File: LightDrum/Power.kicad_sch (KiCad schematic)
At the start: 46 parts, among them Q2 BC807, U26 LM22673-SOIC, U27 LMV324, U28 LMV324, U29 LMV324, U3 LMV324, U39 74HCT2G08, U4 LMV324, U42 INA4181 A2, U43 INA4181 A2, U46 74HC02, U5 LMV324, U6 LM358, U7 OPA1652

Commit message: Add docs and gerbers for REV7
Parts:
- D6: footprint Diode_SMD:D_SMA-SMB_Universal_Handsoldering -> Diode_SMD:D_SMA
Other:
- title: POWER SUPPLY -> LightDrum
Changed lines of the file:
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@@
   (paper "A4")
   (title_block
-    (title "POWER SUPPLY")
-    (rev "REV6")
+    (title "LightDrum")
+    (rev "REV7")
     (company "Daxxn Industries")
   )
@@
       (effects (font (size 1.27 1.27)) (justify left))
     )
-    (property "Footprint" "Diode_SMD:D_SMA-SMB_Universal_Handsoldering" (id 2) (at 91.44 40.64 90)
-      (effects (font (size 1.27 1.27)) hide)
-    )
+    (property "Footprint" "Diode_SMD:D_SMA" (id 2) (at 91.44 40.64 90)
+      (effects (font (size 1.27 1.27)) hide)
+    )

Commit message: First pass over schematic (WIP)
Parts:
- removed C39: 1uF, Capacitor_SMD:C_0603_1608Metric, symbol Device:C_Small
- removed C41, C43, C45, C46, C48, C50, C53, C58, C59, C60, C86: ${D-CAP}, Capacitor_SMD:C_0603_1608Metric, symbol Device:C_Small
- removed Q2: BC807, Package_TO_SOT_SMD:SOT-23, symbol Transistor_BJT:BC807
- removed R104: 1K${RES}, Resistor_SMD:R_0805_2012Metric, symbol Device:R_Small_US
- removed R72: 2.7K${RES}, Resistor_SMD:R_0805_2012Metric, symbol Device:R_Small_US
- removed R73: 7.5K${RES}, Resistor_SMD:R_0805_2012Metric, symbol Device:R_Small_US
- removed U27, U28, U29, U3, U4, U5: LMV324, Package_SO:TSSOP-14_4.4x5mm_P0.65mm, symbol Amplifier_Operational:LMV324
- removed U46: 74HC02, Daxxn_Packages:DHVQFN14, symbol 74xx:74HC02
- removed U6: LM358, Package_SO:TSSOP-8_4.4x3mm_P0.65mm, symbol Amplifier_Operational:LM358
- removed U7: OPA1652, Package_SO:VSSOP-8_3.0x3.0mm_P0.65mm, symbol Daxxn_OPAMP:OPA1652
- added C20: 22pF, Capacitor_SMD:C_0603_1608Metric, symbol Device:C_Small
- added C21, C22: 100nF, Capacitor_SMD:C_0805_2012Metric, symbol Device:C_Small
- added C23, C24: 1uF, Capacitor_SMD:C_0805_2012Metric, symbol Device:C_Small
- added C25: 10uF, Capacitor_SMD:CP_Elec_5x5.4, symbol Device:C_Polarized_Small
- added C26: 100nF, Capacitor_SMD:C_0603_1608Metric, symbol Device:C_Small
- added L1: 2.2uH, symbol Device:L
- added L3: 22uH, Daxxn_Passives:PA4341, symbol Device:L
- added R12: 2.78K, Resistor_SMD:R_0805_2012Metric, symbol Device:R_Small_US
- added R13, R14, R17: 100K, Resistor_SMD:R_0805_2012Metric, symbol Device:R_Small_US
- added R15: 430K, Resistor_SMD:R_0805_2012Metric, symbol Device:R_Small_US
- added R16: 7.5K, Resistor_SMD:R_0805_2012Metric, symbol Device:R_Small_US
- added U3: AP3401, Package_DFN_QFN:DFN-6-1EP_2x2mm_P0.65mm_EP1x1.6mm, symbol Daxxn_Regulators:AP3401
- C49, C55, C62, C63: value ${D-CAP} -> 100nF
- L2: value 22uH -> 10uH; footprint Daxxn_Passives:PA4341 -> Capacitor_SMD:C_1210_3225Metric; now left out of the parts list
- R71: value 15K${RES} -> 15K
- U39: value 74HCT2G08 -> 74HC2G08
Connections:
- net GND: now also C21.2, C22.2, C23.2, C24.2, C25.2, C26.2, R12.1, R17.2, U3.5 (GND), U3.7 (GND)
- net PS-FB_: now also R12.2, R16.1
- net PS-SW_: now also L3.1; no longer L2.1
- net VCC: now also C25.1, C26.1, L3.2, R13.1, R14.1, R16.2, U3.3 (VIN); no longer C55.1, C62.1, C63.1, L2.2, U39.8, U42.5, U43.5
- new net: R14.2, U3.2 (PG)
- new net: R13.2, U3.1 (EN)
- new net: L1.1, U3.4 (LX)
- new net: C20.2, R15.2, R17.1, U3.6 (FB)
- new net +3V3: C20.1, C21.1, C22.1, C23.1, L1.2, L2.1, R15.1
- new net VDD: C24.1, C55.1, C62.1, C63.1, L2.2, U39.8, U42.5, U43.5
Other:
- note added: "3.3V REGULATOR"
- note added: "The new voltage is going to be 3.3V. Need to check all my ICs and confirm compatibility."
- note removed: "2.6K Would be exactly 5V but its hard to find a resistor with that value."
- note removed: "AUDIO AMP"
- note removed: "AUDIO fILTERS"
- note removed: "COUNTER"
- note removed: "ICSP Backfeed Protection"
- note removed: "OR GATE"
- note removed: "PWM MUX CONTROL"
- note removed: "TIMER"
- moved on the sheet: C55, C62, C63, U39C, U42E, U43E

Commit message: General component placement
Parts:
- C1001: renamed from C20; footprint Capacitor_SMD:C_0603_1608Metric -> Capacitor_SMD:C_0402_1005Metric
- D1001: renamed from D6; value ES2A/A -> SK36AHE3
- L1001: renamed from L1; footprint (none) -> Daxxn_Passives:LQH3NPN; now in the parts list
- L1002: renamed from L2; now in the parts list
- L1003: renamed from L3; now in the parts list
- R1001: renamed from R12; now in the parts list
- R1002: renamed from R13; footprint Resistor_SMD:R_0805_2012Metric -> Resistor_SMD:R_0402_1005Metric; now in the parts list
- R1003: renamed from R14; footprint Resistor_SMD:R_0805_2012Metric -> Resistor_SMD:R_0402_1005Metric; now in the parts list
- R1004: renamed from R15; footprint Resistor_SMD:R_0805_2012Metric -> Resistor_SMD:R_0402_1005Metric; now in the parts list
- R1005: renamed from R16; now in the parts list
- R1006: renamed from R17; footprint Resistor_SMD:R_0805_2012Metric -> Resistor_SMD:R_0402_1005Metric; now in the parts list
- U1002: renamed from U26; PartNumber (none) -> 0805-0001; SupplierPN (none) -> LM22673MRE-5.0/NOPBCT-ND
- U701: renamed from U42; PartNumber (none) -> 0815-0003
- U702: renamed from U43; PartNumber (none) -> 0815-0003
- U901: renamed from U39; PartNumber (none) -> 0802-0005
- renumbered C21 to C1002, C22 to C1003, C23 to C1004, C24 to C1005, C38 to C1006, C40 to C1007, C42 to C1008, C56 to C1009, C47 to C1010, C25 to C1011, C26 to C1012, C44 to C1013, C49 to C1014, C51 to C1015, C57 to C1016, C52 to C1017, C54 to C1018, C55 to C1019, C62 to C1020, C63 to C1021, R71 to R1007, U3 to U1001

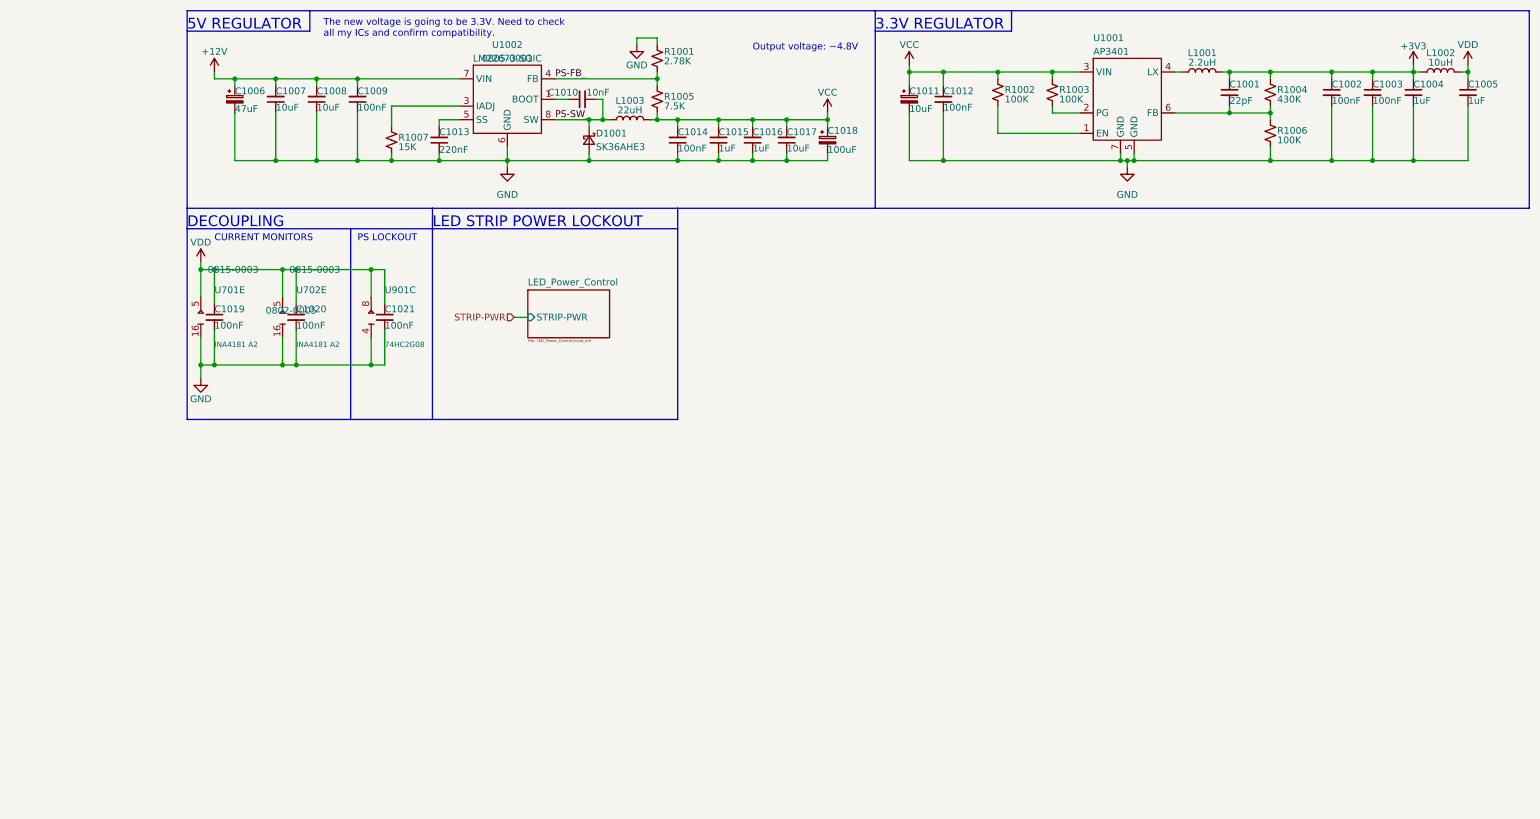
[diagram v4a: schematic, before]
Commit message: Simplify analog power supply and add some routing
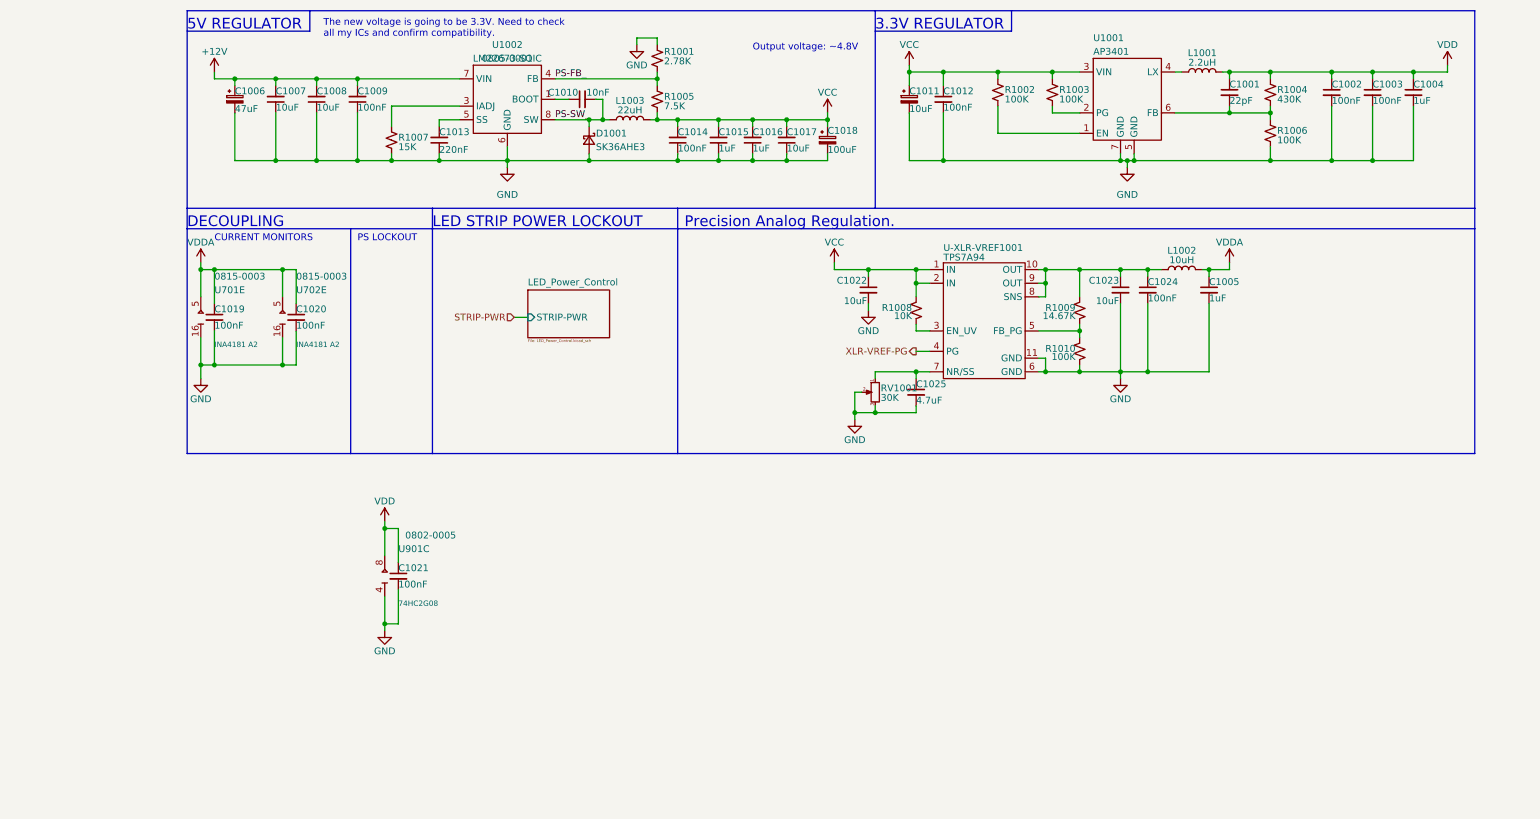
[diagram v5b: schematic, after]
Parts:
- added C1022, C1023: 10uF, Capacitor_SMD:C_1210_3225Metric, symbol Device:C_Small
- added C1024: 100nF, Capacitor_SMD:C_0603_1608Metric, symbol Device:C_Small
- added C1025: 4.7uF, Capacitor_SMD:C_0805_2012Metric, symbol Device:C_Small
- added R1008: 10K, Resistor_SMD:R_0402_1005Metric, symbol Device:R_Small_US
- added R1009: 14.67K, Resistor_SMD:R_0603_1608Metric, symbol Device:R_Small_US
- added R1010: 100K, Resistor_SMD:R_0603_1608Metric, symbol Device:R_Small_US
- added RV1001: 30K, Daxxn_Switches:Bourns_TC33X, symbol Device:R_Potentiometer_Small
- added U-XLR-VREF1001: TPS7A94, Daxxn_Packages:WSON-10-1EP_3x3mm, symbol Daxxn_Regulators:TPS7A94
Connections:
- net GND: now also C1022.2, C1023.2, C1024.2, C1025.2, R1010.2, RV1001.2, RV1001.3, U-XLR-VREF1001.11 (GND), U-XLR-VREF1001.6 (GND)
- net VCC: now also C1022.1, R1008.1, U-XLR-VREF1001.1 (IN), U-XLR-VREF1001.2 (IN)
- net VDD: now also C1001.1, C1002.1, C1003.1, C1004.1, L1001.2, R1004.1; no longer C1005.1, C1019.1, C1020.1, L1002.2, U701.5, U702.5
- removed net +3V3: C1001.1, C1002.1, C1003.1, C1004.1, L1001.2, L1002.1, R1004.1
- new net: C1025.1, RV1001.1, U-XLR-VREF1001.7 (NR/SS)
- new net: C1023.1, C1024.1, L1002.1, R1009.1, U-XLR-VREF1001.10 (OUT), U-XLR-VREF1001.8 (SNS), U-XLR-VREF1001.9 (OUT)
- new net: R1009.2, R1010.1, U-XLR-VREF1001.5 (FB_PG)
- new net: R1008.2, U-XLR-VREF1001.3 (EN_UV)
- new net VDDA: C1005.1, C1019.1, C1020.1, L1002.2, U701.5, U702.5
- new net XLR-VREF-PG: U-XLR-VREF1001.4 (PG)
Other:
- note added: "Precision Analog Regulation."
- moved on the sheet: C1005, C1021, L1002, U901C

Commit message: Swap mcu again... (WIP)
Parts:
- added C?: 10uF, Capacitor_SMD:C_1210_3225Metric, symbol Device:C_Small
- added C? (x12): 100nF, Capacitor_SMD:C_0402_1005Metric, symbol Device:C_Small
- added C?: 10nF, Capacitor_SMD:C_0402_1005Metric, symbol Device:C_Small
- added C? (x2): 1uF, Capacitor_SMD:C_0805_2012Metric, symbol Device:C_Small
- added R?: 47, Resistor_SMD:R_0402_1005Metric, symbol Device:R_Small_US
- added STM?: STM32F446ZCH6, Daxxn_Packages:UFBGA144-7x7xOP6, symbol Daxxn_STMicros:STM32F446ZCH6
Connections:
- net GND: now also C?.2, C?.2, C?.2, C?.2, C?.2, C?.2, C?.2, C?.2, C?.2, C?.2, C?.2, C?.2, C?.2, C?.2, C?.2, C?.2, STM?.D2 (VSS), STM?.E6 (VSS), STM?.E7 (VSS), STM?.G10 (VSS), STM?.G4 (VSS), STM?.G8 (VSS), STM?.H6 (VSS), STM?.J1 (VSSA), STM?.K1 (VREF-)
- net VDD: now also C?.1, C?.1, C?.1, C?.1, C?.1, C?.1, C?.1, C?.1, C?.1, C?.1, C?.1, C?.1, STM?.D3 (VDD), STM?.F10 (VDD), STM?.F4 (VDD), STM?.F5 (VDD), STM?.F6 (VDD), STM?.F7 (VDD), STM?.F8 (VDD), STM?.F9 (VDD), STM?.G5 (VDD), STM?.G6 (VDD), STM?.G7 (VDD)
- net VDDA: now also C?.1, C?.1, C?.1, C?.1, R?.2, STM?.M1 (VDDA)
- new net: R?.1, STM?.L1 (VREF+)
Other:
- moved on the sheet: C1021, U901C

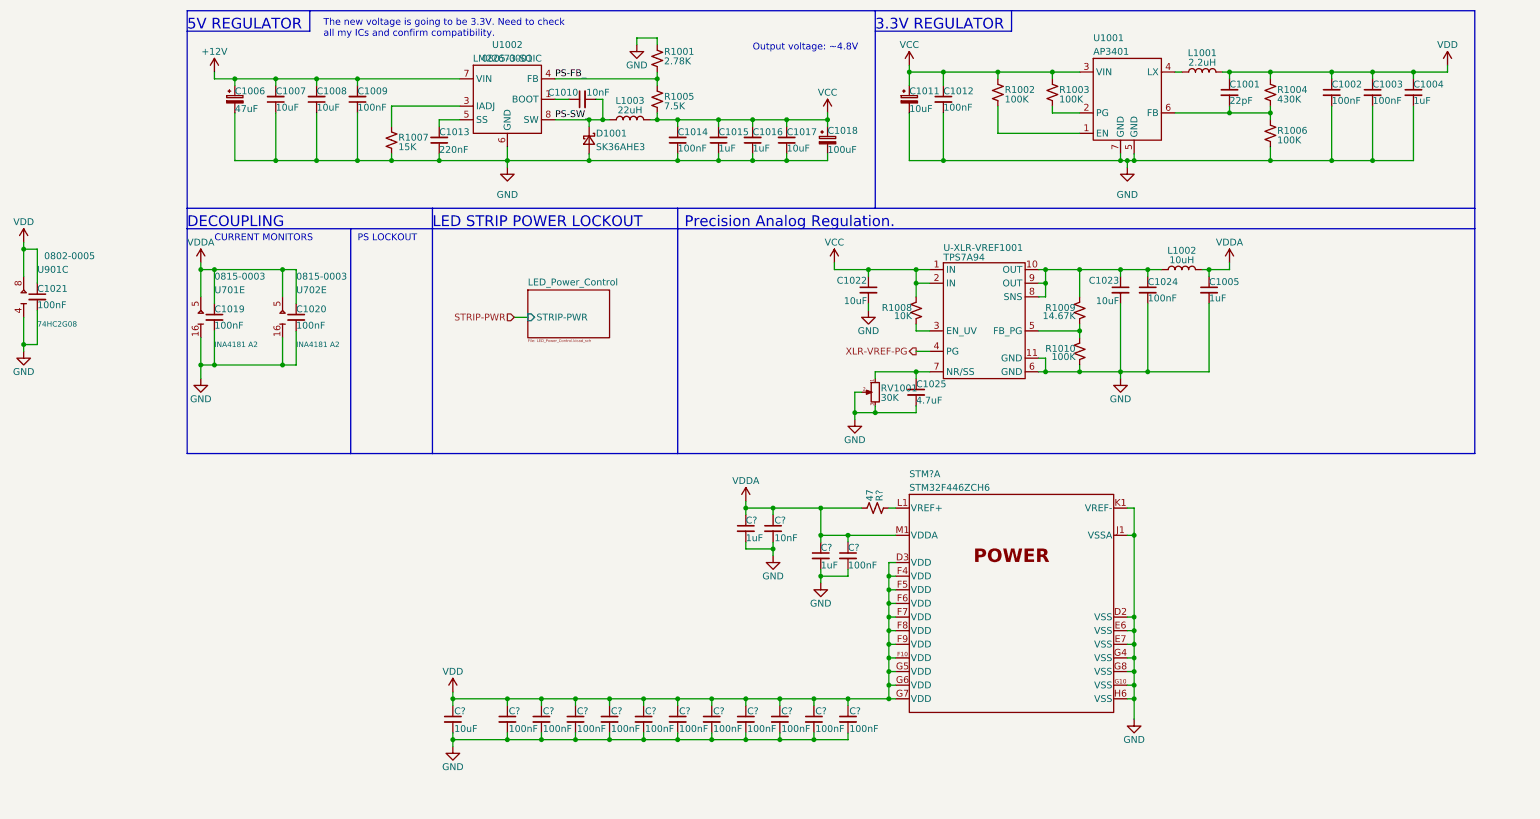
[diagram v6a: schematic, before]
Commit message: Replace barrel jacks with proper DIN4 conn and more
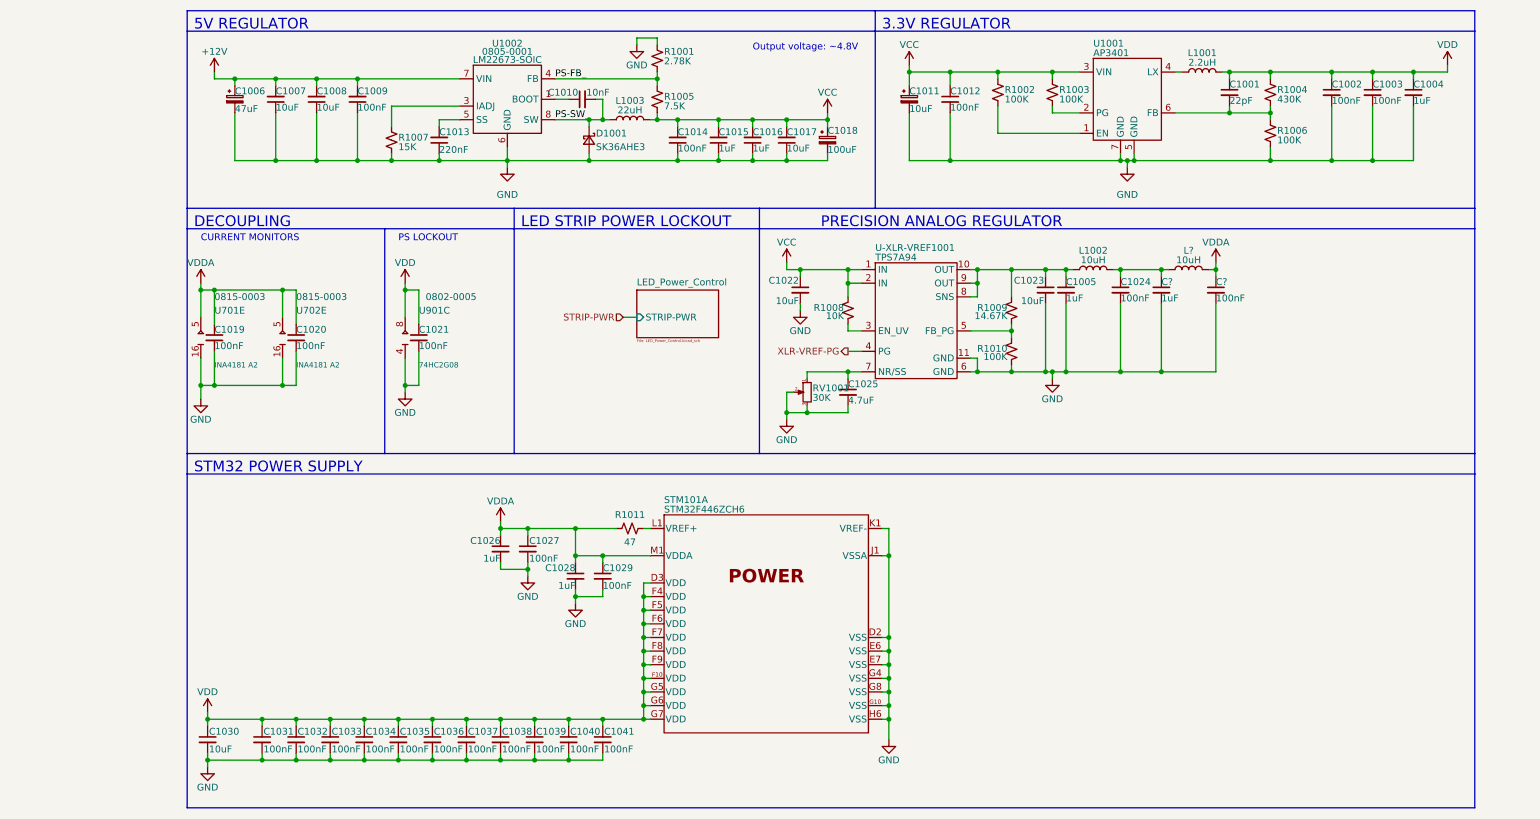
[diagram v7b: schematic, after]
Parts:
- added C?: 1uF, Capacitor_SMD:C_0805_2012Metric, symbol Device:C_Small
- added C?: 100nF, Capacitor_SMD:C_0603_1608Metric, symbol Device:C_Small
- added L?: 10uH, Capacitor_SMD:C_1210_3225Metric, symbol Device:L
- C1027: renamed from C?; value 10nF -> 100nF
- gave numbers to parts that had none: 17
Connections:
- net GND: now also C?.2, C?.2
- net VDDA: now also C?.1, L?.2; no longer C1005.1, L1002.2
- net at C1023.1, L1002.1, R1009.1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: now also C1005.1; no longer C1024.1
- new net: C1024.1, C?.1, L1002.2, L?.1
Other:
- note added: "PRECISION ANALOG REGULATOR"
- note added: "STM32 POWER SUPPLY"
- note removed: "Precision Analog Regulation."
- note removed: "The new voltage is going to be 3.3V. Need to check all my ICs and confirm compatibility."
- moved on the sheet: C1005, C1012, C1019, C1020, C1021, C1022, C1023, C1024, C1025, C1026, C1027, C1028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

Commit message: Replace old MOSFETs with a more compact package
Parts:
- gave numbers to parts that had none: 3
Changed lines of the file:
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@@
   (symbol (lib_id "Device:L") (at 203.2 64.77 90) (unit 1)
     (in_bom yes) (on_board yes)
-    (property "Reference" "L?" (id 0) (at 203.2 61.214 90))
+    (property "Reference" "L1004" (id 0) (at 203.2 61.214 90))
     (property "Value" "10uH" (id 1) (at 203.2 62.992 90))
     (property "Footprint" "Capacitor_SMD:C_1210_3225Metric" (id 2) (at 203.2 64.77 0)
@@
   (symbol (lib_id "Device:C_Small") (at 198.12 68.58 0) (unit 1)
     (in_bom yes) (on_board yes)
-    (property "Reference" "C?" (id 0) (at 198.12 67.056 0)
+    (property "Reference" "C1042" (id 0) (at 198.12 67.056 0)
       (effects (font (size 1.27 1.27)) (justify left))
     )
@@
   (symbol (lib_id "Device:C_Small") (at 208.28 68.58 0) (unit 1)
     (in_bom yes) (on_board yes)
-    (property "Reference" "C?" (id 0) (at 208.28 67.056 0)
-      (effects (font (size 1.27 1.27)) (justify left))
-    )
+    (property "Reference" "C1043" (id 0) (at 208.28 67.056 0)
+      (effects (font (size 1.27 1.27)) (justify left))
+    )
